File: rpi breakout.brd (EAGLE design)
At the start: 114 x 102.9 mm, 51 parts, among them IC1 PCA9505, J1 RASPBERRYPI-40-PIN-GPIO_PTH, U1 MAX11642EEG, U2 MAX11642EEG, U3 MAX11642EEG

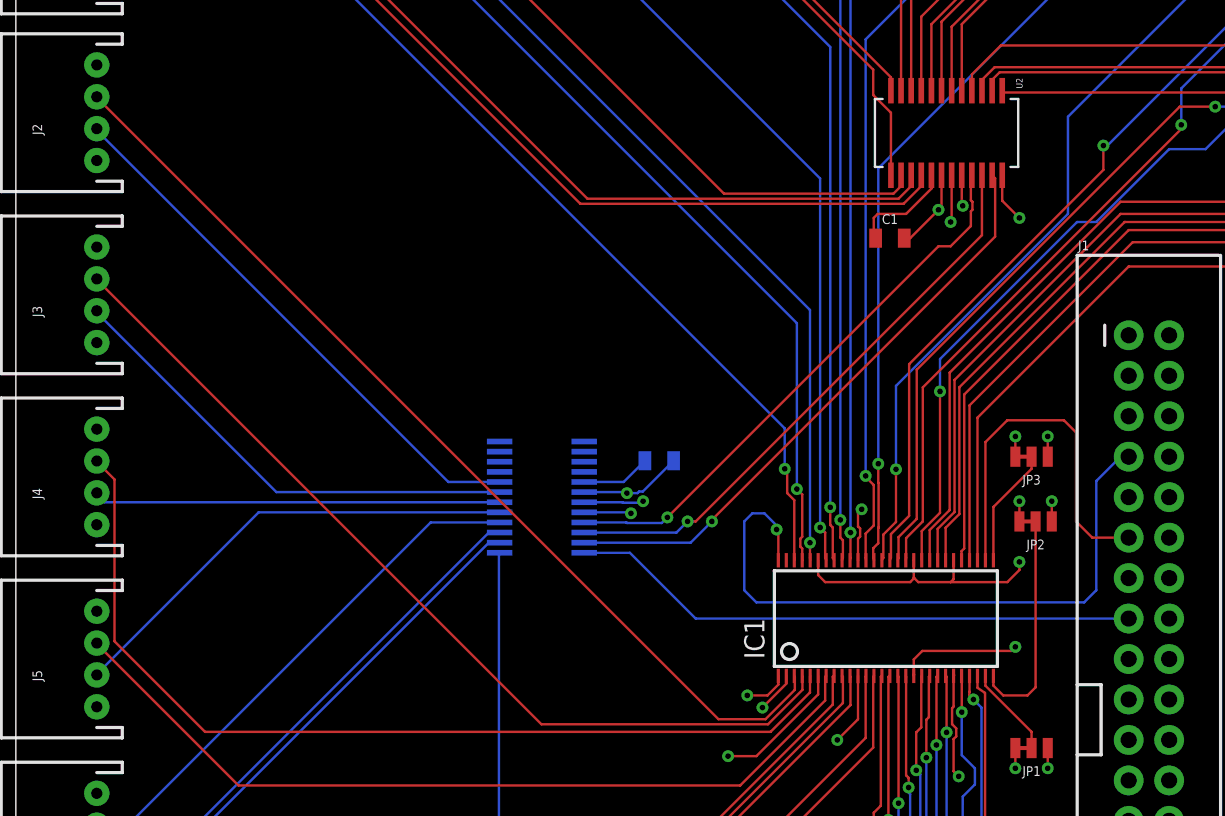
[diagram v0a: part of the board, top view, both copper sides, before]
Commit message: pulled OE and Reset lines to 5v and ground
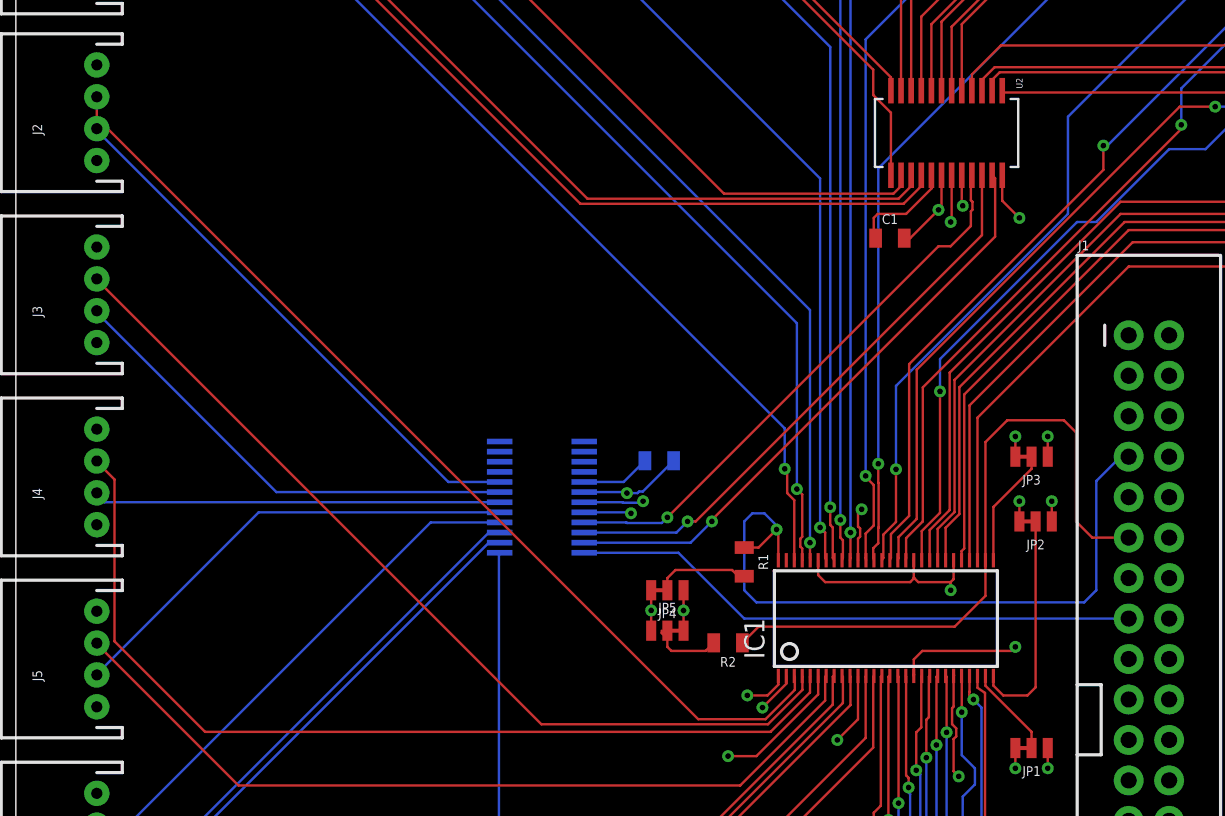
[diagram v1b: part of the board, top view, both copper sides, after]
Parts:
- added JP4, JP5: JUMPER-SMT_3_1-NC_TRACE_NO-SILK, SparkFun-Jumpers:SMT-JUMPER_3_1-NC_TRACE_NO-SILK
- added R1, R2: (no value), SparkFun-Resistors:0805
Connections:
- new net N$1: JP4.2, R1.2
- new net N$4: JP5.2, R2.2
- net !RESET: now also R1.1
- net 5V: now also JP4.3, JP5.1
- net GND: now also JP4.1, JP5.3
- net OE: now also R2.1
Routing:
- net OE: track 23.3 -> 42.0 mm
- net N$1: track 0.00 -> 6.11 mm
- net N$4: track 0.00 -> 4.39 mm
- net 5V: track 27.3 -> 29.8 mm, vias 8 -> 9
- net !RESET: track 41.4 -> 43.9 mm
- net GND: track 58.5 -> 56.4 mm, vias 11 -> 12
- net DIO1: track 61.7 -> 62.4 mm
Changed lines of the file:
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@@
 <attribute name="VALUE" x="40.386" y="60.325" size="0.6096" layer="28" font="vector" ratio="20" rot="MR180" align="top-center"/>
+</element>
+<element name="R1" library="SparkFun-Resistors" library_urn="urn:adsk.eagle:library:532" package="0805" package3d_urn="urn:adsk.eagle:package:39651/1" value=" " x="45.72" y="53.086" smashed="yes" rot="R270">
+<attribute name="NAME" x="46.609" y="53.086" size="0.6096" layer="25" font="vector" ratio="20" rot="R270" align="bottom-center"/>
+<attribute name="PROD_ID" value=" " x="45.72" y="53.086" size="1.778" layer="27" rot="R270" display="off"/>
+<attribute name="VALUE" x="44.831" y="53.086" size="0.6096" layer="27" font="vector" ratio="20" rot="R270" align="top-center"/>
+</element>
+<element name="R2" library="SparkFun-Resistors" library_urn="urn:adsk.eagle:library:532" package="0805" package3d_urn="urn:adsk.eagle:package:39651/1" value=" " x="44.704" y="48.006" smashed="yes" rot="R180">
+<attribute name="NAME" x="44.704" y="47.117" size="0.6096" layer="25" font="vector" ratio="20" rot="R180" align="bottom-center"/>
+<attribute name="PROD_ID" value=" " x="44.704" y="48.006" size="1.778" layer="27" rot="R180" display="off"/>
+<attribute name="VALUE" x="44.704" y="48.895" size="0.6096" layer="27" font="vector" ratio="20" rot="R180" align="top-center"/>
+</element>
+<element name="JP4" library="SparkFun-Jumpers" library_urn="urn:adsk.eagle:library:528" package="SMT-JUMPER_3_1-NC_TRACE_NO-SILK" package3d_urn="urn:adsk.eagle:package:39287/1" value="JUMPER-SMT_3_1-NC_TRACE_NO-SILK" x="40.894" y="51.308" smashed="yes" rot="R180">
+<attribute name="NAME" x="40.894" y="50.165" size="0.6096" layer="25" font="vector" ratio="20" rot="R180" align="bottom-center"/>
+<attribute name="VALUE" x="40.894" y="52.451" size="0.6096" layer="27" font="vector" ratio="20" rot="R180" align="top-center"/>
+</element>
+<element name="JP5" library="SparkFun-Jumpers" library_urn="urn:adsk.eagle:library:528" package="SMT-JUMPER_3_1-NC_TRACE_NO-SILK" package3d_urn="urn:adsk.eagle:package:39287/1" value="JUMPER-SMT_3_1-NC_TRACE_NO-SILK" x="40.894" y="48.768" smashed="yes">
+<attribute name="NAME" x="40.894" y="49.911" size="0.6096" layer="25" font="vector" ratio="20" align="bottom-center"/>
+<attribute name="VALUE" x="40.894" y="47.625" size="0.6096" layer="27" font="vector" ratio="20" align="top-center"/>
 </element>
 </elements>
@@
 <wire x1="58.674" y1="51.816" x2="56.642" y2="51.816" width="0.1524" layer="1"/>
 <wire x1="56.642" y1="51.816" x2="56.388" y2="52.07" width="0.1524" layer="1"/>
-<wire x1="58.674" y1="51.816" x2="62.23" y2="51.816" width="0.1524" layer="1"/>
-<wire x1="62.992" y1="52.578" x2="62.23" y2="51.816" width="0.1524" layer="1"/>
-<via x="62.992" y="53.086" extent="1-16" drill="0.35"/>
-<wire x1="62.992" y1="53.086" x2="62.992" y2="52.578" width="0.1524" layer="1"/>
+<via x="58.674" y="51.308" extent="1-16" drill="0.35"/>
+<wire x1="58.674" y1="51.308" x2="58.674" y2="51.816" width="0.1524" layer="1"/>
 <contactref element="C2" pad="2"/>
 <contactref element="C1" pad="2"/>
@@
 <via x="87.376" y="40.894" extent="1-16" drill="0.35"/>
 <wire x1="87.376" y1="38.238" x2="87.376" y2="40.894" width="0.1524" layer="1"/>
+<contactref element="JP5" pad="3"/>
+<contactref element="JP4" pad="1"/>
+<via x="41.91" y="50.038" extent="1-16" drill="0.35"/>
+<wire x1="41.91" y1="48.768" x2="41.91" y2="50.038" width="0.1524" layer="1"/>
+<wire x1="41.91" y1="50.038" x2="41.91" y2="51.308" width="0.1524" layer="1"/>
 </signal>
 <signal name="5V">
@@
 <wire x1="62.484" y1="47.498" x2="62.738" y2="47.752" width="0.1524" layer="1"/>
 <via x="62.738" y="47.752" extent="1-16" drill="0.35"/>
+<contactref element="JP4" pad="3"/>
+<contactref element="JP5" pad="1"/>
+<via x="39.878" y="50.038" extent="1-16" drill="0.35"/>
+<wire x1="39.878" y1="51.308" x2="39.878" y2="50.038" width="0.1524" layer="1"/>
+<wire x1="39.878" y1="50.038" x2="39.878" y2="48.768" width="0.1524" layer="1"/>
 </signal>
 <signal name="SDA">
@@
 <wire x1="67.818" y1="58.166" x2="69.342" y2="59.69" width="0.1524" layer="16"/>
 <wire x1="69.342" y1="59.69" x2="69.85" y2="59.69" width="0.1524" layer="16"/>
+<contactref element="R1" pad="1"/>
+<wire x1="45.72" y1="53.986" x2="46.62" y2="53.986" width="0.1524" layer="1"/>
+<wire x1="46.62" y1="53.986" x2="47.752" y2="55.118" width="0.1524" layer="1"/>
 </signal>
 <signal name="INT">
@@
 <wire x1="66.548" y1="55.626" x2="67.564" y2="54.61" width="0.1524" layer="1"/>
 <wire x1="67.564" y1="54.61" x2="69.85" y2="54.61" width="0.1524" layer="1"/>
+<contactref element="R2" pad="1"/>
+<wire x1="45.604" y1="48.006" x2="46.62" y2="49.022" width="0.1524" layer="1"/>
+<wire x1="46.62" y1="49.022" x2="58.928" y2="49.022" width="0.1524" layer="1"/>
+<wire x1="58.928" y1="49.022" x2="60.86" y2="50.954" width="0.1524" layer="1"/>
+<wire x1="60.86" y1="50.954" x2="60.86" y2="53.19" width="0.1524" layer="1"/>
 </signal>
 <signal name="N$17">
@@
 <wire x1="48.895" y1="45.05325" x2="48.895" y2="45.87875" width="0.1524" layer="1"/>
 <wire x1="47.0535" y1="43.21175" x2="48.895" y2="45.05325" width="0.1524" layer="1"/>
-<wire x1="44.10075" y1="43.21175" x2="47.0535" y2="43.21175" width="0.1524" layer="1"/>
-<wire x1="5.08" y1="82.2325" x2="44.10075" y2="43.21175" width="0.1524" layer="1"/>
+<wire x1="42.83075" y1="43.21175" x2="47.0535" y2="43.21175" width="0.1524" layer="1"/>
+<wire x1="5.08" y1="80.9625" x2="42.83075" y2="43.21175" width="0.1524" layer="1"/>
 <wire x1="48.895" y1="45.87875" x2="48.86" y2="45.93" width="0.1524" layer="1"/>
-<wire x1="5.08" y1="82.2325" x2="5.08" y2="82.28" width="0.1524" layer="1"/>
+<wire x1="5.08" y1="80.9625" x2="5.08" y2="82.28" width="0.1524" layer="1"/>
 </signal>
 <signal name="AD1">
@@
 <contactref element="U3" pad="24"/>
 <contactref element="J1" pad="15"/>
-<wire x1="69.85" y1="49.53" x2="42.672" y2="49.53" width="0.1524" layer="16"/>
-<wire x1="38.5445" y1="53.6575" x2="35.6743" y2="53.6575" width="0.1524" layer="16"/>
-<wire x1="42.672" y1="49.53" x2="38.5445" y2="53.6575" width="0.1524" layer="16"/>
+<wire x1="69.85" y1="49.53" x2="45.72" y2="49.53" width="0.1524" layer="16"/>
+<wire x1="41.5925" y1="53.6575" x2="35.6743" y2="53.6575" width="0.1524" layer="16"/>
+<wire x1="45.72" y1="49.53" x2="41.5925" y2="53.6575" width="0.1524" layer="16"/>
 </signal>
 <signal name="CS3">
@@
 <contactref element="J1" pad="17"/>
 </signal>
+<signal name="N$1">
+<contactref element="R1" pad="2"/>
+<contactref element="JP4" pad="2"/>
+<wire x1="45.72" y1="52.186" x2="45.535" y2="52.001" width="0.1524" layer="1"/>
+<wire x1="40.894" y1="51.308" x2="40.894" y2="52.07" width="0.1524" layer="1"/>
+<wire x1="40.894" y1="52.07" x2="41.402" y2="52.578" width="0.1524" layer="1"/>
+<wire x1="41.402" y1="52.578" x2="44.958" y2="52.578" width="0.1524" layer="1"/>
+<wire x1="44.958" y1="52.578" x2="45.535" y2="52.001" width="0.1524" layer="1"/>
+</signal>
+<signal name="N$4">
+<contactref element="R2" pad="2"/>
+<contactref element="JP5" pad="2"/>
+<wire x1="43.804" y1="48.006" x2="43.296" y2="47.498" width="0.1524" layer="1"/>
+<wire x1="43.296" y1="47.498" x2="41.148" y2="47.498" width="0.1524" layer="1"/>
+<wire x1="41.148" y1="47.498" x2="40.894" y2="47.752" width="0.1524" layer="1"/>
+<wire x1="40.5384" y1="48.6207" x2="40.5384" y2="48.768" width="0.1524" layer="1"/>
+<wire x1="40.894" y1="47.752" x2="40.894" y2="48.2651" width="0.1524" layer="1"/>
+<wire x1="40.894" y1="48.2651" x2="40.5384" y2="48.6207" width="0.1524" layer="1"/>
+<wire x1="40.5384" y1="48.768" x2="40.894" y2="48.768" width="0" layer="19" extent="1-1"/>
+</signal>
 </signals>

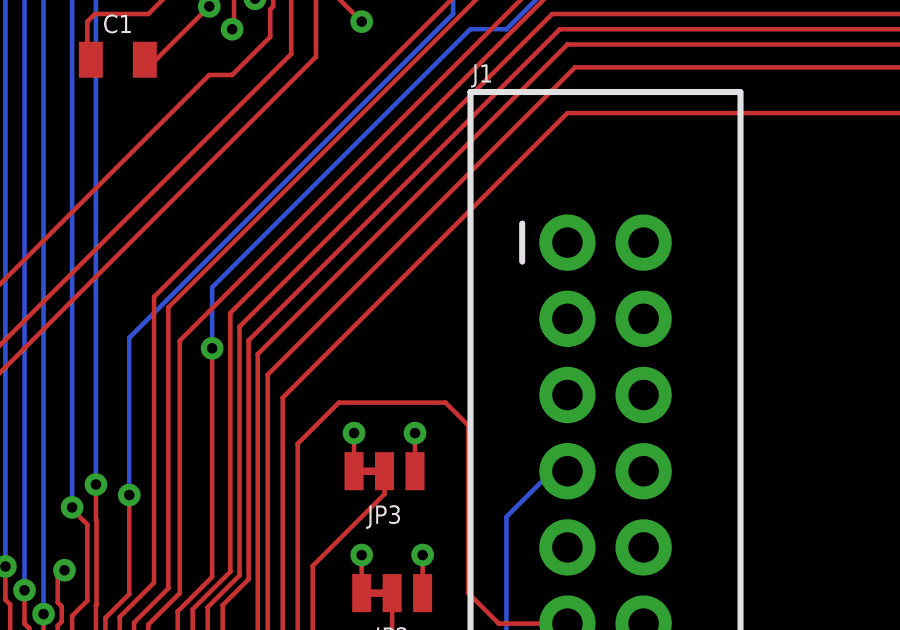
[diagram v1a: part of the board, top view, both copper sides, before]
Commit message: added i2c pull ups
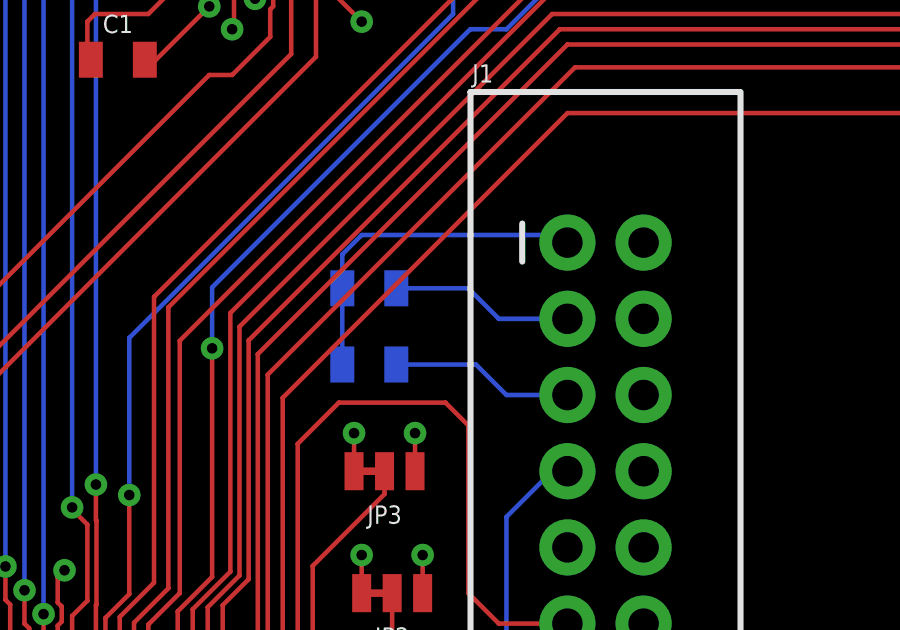
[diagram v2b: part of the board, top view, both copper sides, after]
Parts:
- added R3, R4: (no value), SparkFun-Resistors:0805
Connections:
- net 3V: now also R3.2, R4.2
- net SCL: now also R4.1
- net SDA: now also R3.1
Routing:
- net 3V: track 0.00 -> 11.5 mm
- net SDA: track 52.0 -> 58.1 mm
- net SCL: track 33.9 -> 40.0 mm
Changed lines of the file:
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@@
 <attribute name="VALUE" x="40.894" y="47.625" size="0.6096" layer="27" font="vector" ratio="20" align="top-center"/>
+</element>
+<element name="R3" library="SparkFun-Resistors" library_urn="urn:adsk.eagle:library:532" package="0805" package3d_urn="urn:adsk.eagle:package:39651/1" value=" " x="63.246" y="65.786" smashed="yes" rot="MR0">
+<attribute name="NAME" x="63.246" y="66.675" size="0.6096" layer="26" font="vector" ratio="20" rot="MR0" align="bottom-center"/>
+<attribute name="PROD_ID" value=" " x="63.246" y="65.786" size="1.778" layer="28" rot="MR0" display="off"/>
+<attribute name="VALUE" x="63.246" y="64.897" size="0.6096" layer="28" font="vector" ratio="20" rot="MR0" align="top-center"/>
+</element>
+<element name="R4" library="SparkFun-Resistors" library_urn="urn:adsk.eagle:library:532" package="0805" package3d_urn="urn:adsk.eagle:package:39651/1" value=" " x="63.246" y="63.246" smashed="yes" rot="MR0">
+<attribute name="NAME" x="63.246" y="64.135" size="0.6096" layer="26" font="vector" ratio="20" rot="MR0" align="bottom-center"/>
+<attribute name="PROD_ID" value=" " x="63.246" y="63.246" size="1.778" layer="28" rot="MR0" display="off"/>
+<attribute name="VALUE" x="63.246" y="62.357" size="0.6096" layer="28" font="vector" ratio="20" rot="MR0" align="top-center"/>
 </element>
 </elements>
@@
 <signal name="3V">
 <contactref element="J1" pad="1"/>
+<contactref element="R3" pad="2"/>
+<contactref element="R4" pad="2"/>
+<wire x1="62.346" y1="63.246" x2="62.346" y2="65.786" width="0.1524" layer="16"/>
+<wire x1="62.346" y1="65.786" x2="62.346" y2="66.918" width="0.1524" layer="16"/>
+<wire x1="62.346" y1="66.918" x2="62.992" y2="67.564" width="0.1524" layer="16"/>
+<wire x1="62.992" y1="67.564" x2="69.596" y2="67.564" width="0.1524" layer="16"/>
+<wire x1="69.596" y1="67.564" x2="69.85" y2="67.31" width="0.1524" layer="16"/>
 </signal>
 <signal name="GND">
@@
 <wire x1="44.958" y1="64.77" x2="40.2872" y2="60.0992" width="0.1524" layer="15"/>
 <wire x1="40.2872" y1="50.3273" x2="45.9105" y2="44.704" width="0.1524" layer="15"/>
+<contactref element="R3" pad="1"/>
+<wire x1="69.85" y1="64.77" x2="67.564" y2="64.77" width="0.1524" layer="16"/>
+<wire x1="67.564" y1="64.77" x2="66.548" y2="65.786" width="0.1524" layer="16"/>
+<wire x1="66.548" y1="65.786" x2="64.146" y2="65.786" width="0.1524" layer="16"/>
 </signal>
 <signal name="SCL">
@@
 <wire x1="64.4172" y1="57.14735" x2="64.4172" y2="56.7972" width="0.1524" layer="2"/>
 <wire x1="64.4172" y1="56.7972" x2="51.562" y2="43.942" width="0.1524" layer="2"/>
+<contactref element="R4" pad="1"/>
+<wire x1="69.85" y1="62.23" x2="67.818" y2="62.23" width="0.1524" layer="16"/>
+<wire x1="67.818" y1="62.23" x2="66.802" y2="63.246" width="0.1524" layer="16"/>
+<wire x1="66.802" y1="63.246" x2="64.146" y2="63.246" width="0.1524" layer="16"/>
 </signal>
 <signal name="!RESET">
